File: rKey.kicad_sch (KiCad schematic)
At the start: 35 parts, among them IC1 7805, J1 Conn_01x06, Q1 BC337, Q2 BC337, Q3 BC337, Q4 BC337, Q5 BC327, Q6 BC337, Q7 BC337, Q8 BC337, U1 TL084BCN, U2 TL084BCN

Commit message: fix: small changes in footprint associations
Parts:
- JB1, JB2: footprint Connector_PinHeader_2.54mm:PinHeader_1x01_P2.54mm_Vertical -> Connector_Wire:SolderWire-0.25sqmm_1x01_D0.65mm_OD1.7mm
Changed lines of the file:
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@@
       (effects (font (size 1.27 1.27)) (justify left) hide)
     )
-    (property "Footprint" "Connector_PinHeader_2.54mm:PinHeader_1x01_P2.54mm_Vertical" (id 2) (at 226.695 47.625 0)
+    (property "Footprint" "Connector_Wire:SolderWire-0.25sqmm_1x01_D0.65mm_OD1.7mm" (id 2) (at 226.695 47.625 0)
       (effects (font (size 1.27 1.27)) hide)
     )
@@
       (effects (font (size 1.27 1.27)) (justify left) hide)
     )
-    (property "Footprint" "Connector_PinHeader_2.54mm:PinHeader_1x01_P2.54mm_Vertical" (id 2) (at 226.695 50.8 0)
+    (property "Footprint" "Connector_Wire:SolderWire-0.25sqmm_1x01_D0.65mm_OD1.7mm" (id 2) (at 226.695 50.8 0)
       (effects (font (size 1.27 1.27)) hide)
     )
@@
     )
     (path "/11708a30-c91b-488f-863d-ad12f67b2667"
-      (reference "JB1") (unit 1) (value "Conn_01x01") (footprint "Connector_PinHeader_2.54mm:PinHeader_1x01_P2.54mm_Vertical")
+      (reference "JB1") (unit 1) (value "Conn_01x01") (footprint "Connector_Wire:SolderWire-0.25sqmm_1x01_D0.65mm_OD1.7mm")
     )
     (path "/d08ed67d-1982-43cb-9cfe-2962c7845c1d"
-      (reference "JB2") (unit 1) (value "Conn_01x01") (footprint "Connector_PinHeader_2.54mm:PinHeader_1x01_P2.54mm_Vertical")
+      (reference "JB2") (unit 1) (value "Conn_01x01") (footprint "Connector_Wire:SolderWire-0.25sqmm_1x01_D0.65mm_OD1.7mm")
     )
     (path "/14ba7033-cfbd-4a12-a6b6-d2854f5d2505"

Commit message: Preliminary version
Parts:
- removed JB1, JB2: Conn_01x01, Connector_Wire:SolderWire-0.25sqmm_1x01_D0.65mm_OD1.7mm, symbol Connector_Generic:Conn_01x01
- added R11, R12, R14, R15, R16, R17: 100K, Resistor_THT:R_Axial_DIN0207_L6.3mm_D2.5mm_P10.16mm_Horizontal, symbol Device:R
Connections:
- net GND: now also R11.2, R12.2, R14.2, R15.2, R16.2, R17.2
- net at Q4.2 (B), R5.2, debug_conn1.4 (Pin_4): now also R12.1
- net at D1.1 (K), Q1.2 (B), R2.2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: now also R15.1
- net at Q2.2 (B), R3.2, debug_conn1.2 (Pin_2): now also R17.1
- net at J1.1 (Pin_1), Keylocker1.7 (Pin_7), R1.1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: now also debug_conn1.7 (Pin_7)
- net at Q6.2 (B), R7.2, debug_conn1.5 (Pin_5): now also R11.1
- net at Q3.2 (B), R4.2, debug_conn1.3 (Pin_3): now also R16.1
- net at Q7.2 (B), R8.2, debug_conn1.6 (Pin_6): now also R14.1

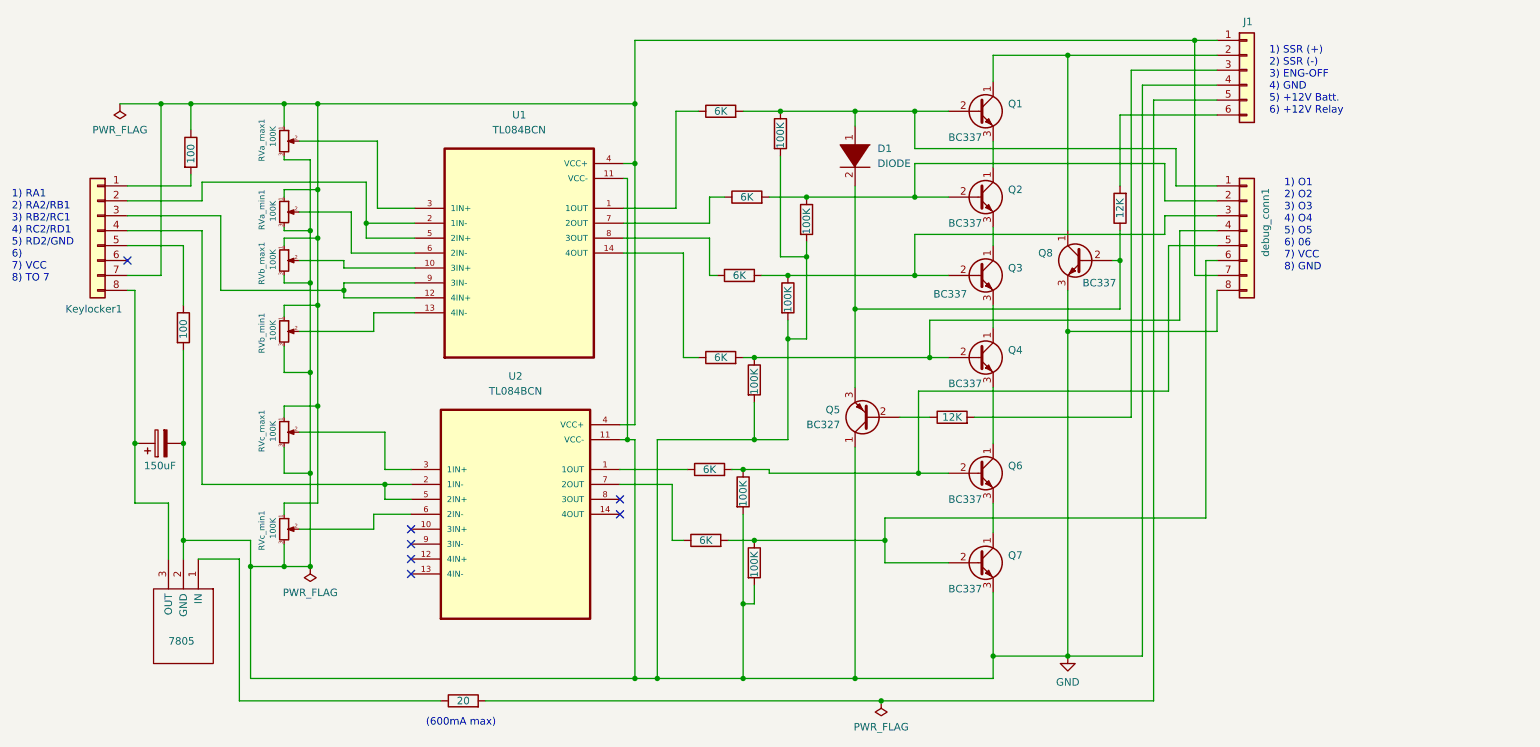
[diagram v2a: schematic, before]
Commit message: Two resistors version
Because in the interdiction zone, the TL084 ount is not zero but 1.5v, I have
added a zenner diode at everey TL084's out. I have also added pull-down
resistors to get a more stable sistuation. But, in order to avoid to use a
bigger PCB, I have bive up to a resistor in the locker key. It reduce the
security level, at the end. But it remain hugh enough.
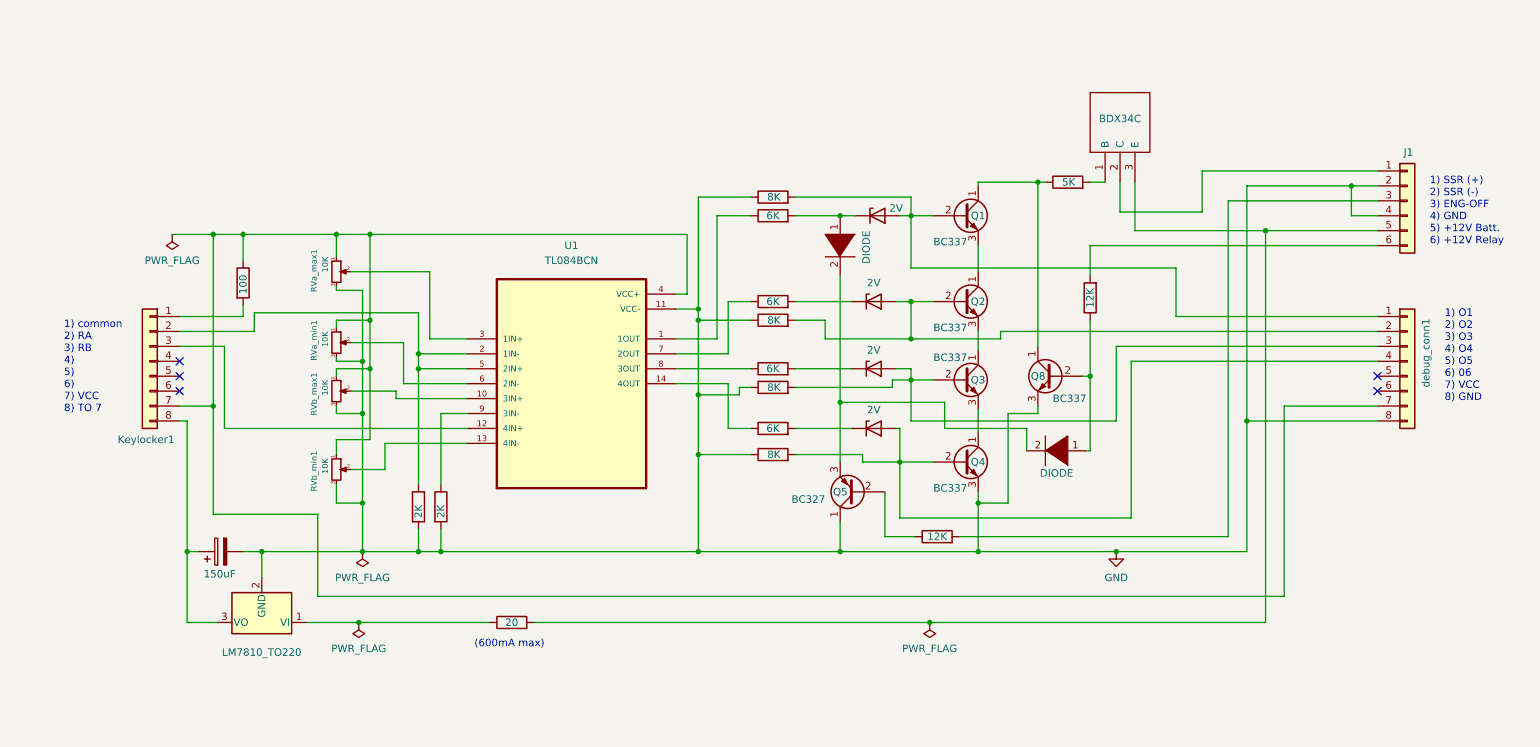
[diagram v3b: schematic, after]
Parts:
- removed IC1: 7805, KiCad:TO254P470X1000X1610-3P, symbol 7805:7805
- removed Q6, Q7: BC337, Package_TO_SOT_THT:TO-92L_Inline_Wide, symbol Transistor_BJT:BC337
- removed R11, R14: 100K, Resistor_THT:R_Axial_DIN0207_L6.3mm_D2.5mm_P10.16mm_Horizontal, symbol Device:R
- removed RVc_max1, RVc_min1: 100K, Potentiometer_THT:Potentiometer_Bourns_3296W_Vertical, symbol Device:R_Potentiometer_Small
- removed U2: TL084BCN, Package_DIP:DIP-14_W7.62mm_LongPads, symbol TL084:TL084BCN
- added D6: DIODE, Diode_THT:D_DO-34_SOD68_P10.16mm_Horizontal, symbol pspice:DIODE
- added IC1: BDX34C, BDX34C:TO270P460X1020X2008-3P, symbol BDX34C:BDX34C
- added U2: LM7810_TO220, Package_TO_SOT_THT:TO-220-3_Vertical, symbol Regulator_Linear:LM7810_TO220
- added ZD2, ZD3, ZD4, ZD5: 2V, Diode_THT:D_DO-34_SOD68_P10.16mm_Horizontal, symbol Device:D_Zener
- J1: footprint Connector_PinHeader_2.54mm:PinHeader_1x06_P2.54mm_Vertical -> Connector_Wire:SolderWire-0.5sqmm_1x06_P4.6mm_D0.9mm_OD2.1mm
- R10: value 100 -> 5K
- R12, R15, R16, R17: value 100K -> 8K
- R7, R8: value 6K -> 2K
- RVa_max1, RVa_min1, RVb_max1, RVb_min1: value 100K -> 10K
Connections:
- net GND: now also J1.2 (Pin_2), Q4.3 (E), R12.1, R15.1, R16.1, R17.1, R7.2, R8.2, U2.2 (GND); no longer R10.2, R12.2, R15.2, R16.2, R17.2
- net at Q4.2 (B), debug_conn1.4 (Pin_4): now also R12.2, ZD4.2 (A); no longer R12.1, R5.2
- net at D1.2 (A), Q5.3 (E): now also D6.2 (A); no longer Q8.2 (B), R9.1
- net at Q2.2 (B), debug_conn1.2 (Pin_2): now also R17.2, ZD2.2 (A); no longer R17.1, R3.2
- net at Keylocker1.2 (Pin_2), U1.2 (1IN-), U1.5 (2IN+): now also R7.1
- net at Keylocker1.3 (Pin_3), U1.12 (4IN+): no longer U1.9 (3IN-)
- net at Keylocker1.5 (Pin_5): no longer R10.1
- net at Keylocker1.7 (Pin_7), R1.1, RVa_max1.1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: no longer J1.1 (Pin_1)
- net at C1.1, Keylocker1.8 (Pin_8): now also U2.3 (VO)
- net at debug_conn1.5 (Pin_5): no longer R7.2
- net at Q3.2 (B), debug_conn1.3 (Pin_3): now also R16.2, ZD3.2 (A); no longer R16.1, R4.2
- net at debug_conn1.6 (Pin_6): no longer R8.2
- net at Q1.1 (C), Q8.1 (C): now also R10.1; no longer J1.2 (Pin_2)
- net at R6.1: now also U2.1 (VI)
- net at R8.1: now also U1.9 (3IN-)
- net at J1.5 (Pin_5), R6.2: now also IC1.3 (E)
- new net: R5.2, ZD4.1 (K)
- new net: D1.1 (K), R2.2, ZD5.1 (K)
- new net: R4.2, ZD3.1 (K)
- new net: D6.1 (K), Q8.2 (B), R9.1
- new net: R3.2, ZD2.1 (K)
- new net: Q1.2 (B), R15.2, ZD5.2 (A), debug_conn1.1 (Pin_1)
- new net: IC1.1 (B), R10.2
- new net: IC1.2 (C), J1.1 (Pin_1)
- no-connect marks 7 -> 5
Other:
- note added: "1) common 2) RA 3) RB 4) 5) 6) 7) VCC 8) TO 7"
- note removed: "1) RA1 2) RA2/RB1 3) RB2/RC1 4) RC2/RD1 5) RD2/GND 6) 7) VCC 8) TO 7"
- moved on the sheet: J1, Keylocker1, Q1, Q2, Q3, Q4, Q5, Q8, RVa_max1, RVa_min1, RVb_max1, RVb_min1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

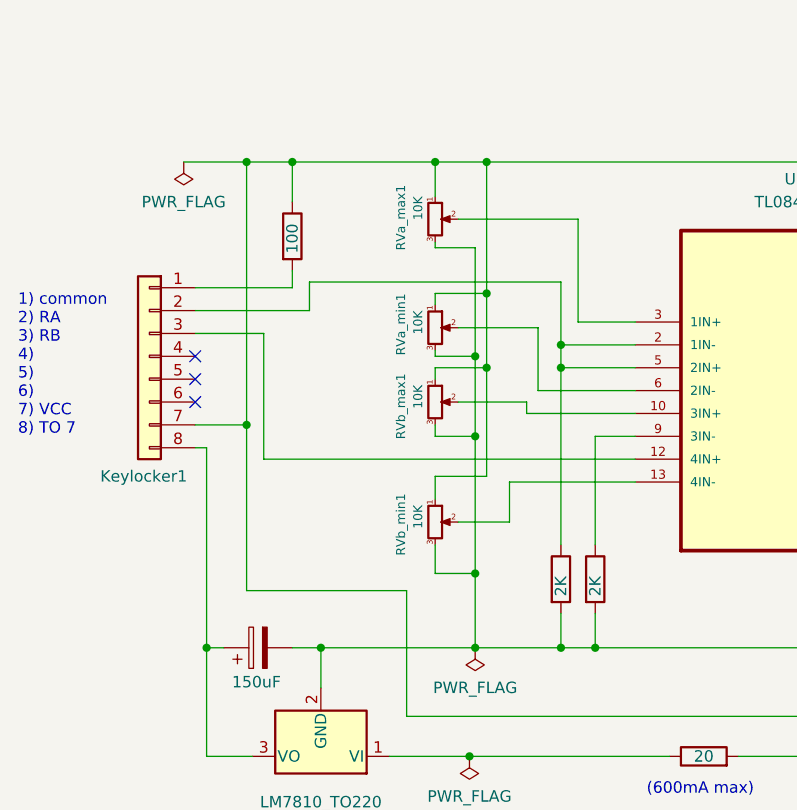
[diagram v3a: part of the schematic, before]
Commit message: Fixes and PCB size reduction
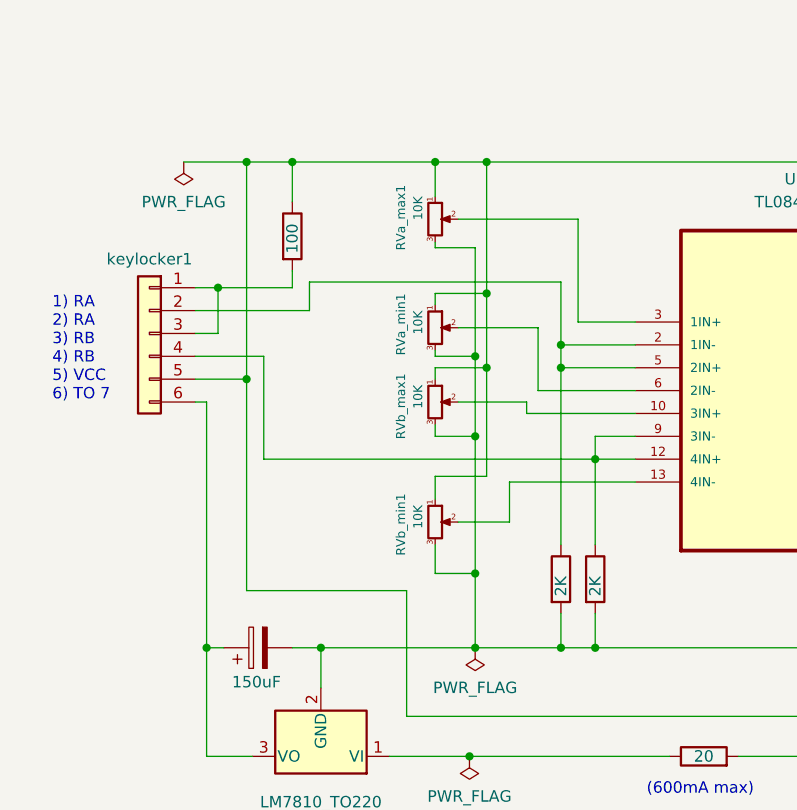
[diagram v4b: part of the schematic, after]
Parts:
- removed Keylocker1: Conn_01x08, Connector_PinHeader_2.54mm:PinHeader_1x08_P2.54mm_Vertical, symbol Connector_Generic:Conn_01x08
- added keylocker1: Conn_01x06, Connector_PinHeader_2.54mm:PinHeader_1x06_P2.54mm_Vertical, symbol Connector_Generic:Conn_01x06
- R6: footprint Resistor_THT:R_Axial_DIN0207_L6.3mm_D2.5mm_P10.16mm_Horizontal -> Resistor_THT:R_Axial_Power_L20.0mm_W6.4mm_P22.40mm
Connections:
- net at R1.2: now also keylocker1.1 (Pin_1), keylocker1.3 (Pin_3)
- net at R7.1, U1.2 (1IN-), U1.5 (2IN+): now also keylocker1.2 (Pin_2)
- net at U1.12 (4IN+): now also R8.1, U1.9 (3IN-), keylocker1.4 (Pin_4)
- net at R1.1, RVa_max1.1, RVa_min1.1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: now also keylocker1.5 (Pin_5)
- net at C1.1, U2.3 (VO): now also keylocker1.6 (Pin_6)
- no-connect marks 5 -> 2
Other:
- note added: "1) RA 2) RA 3) RB 4) RB 5) VCC 6) TO 7"
- note removed: "1) common 2) RA 3) RB 4) 5) 6) 7) VCC 8) TO 7"
